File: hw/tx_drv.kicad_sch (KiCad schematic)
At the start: 7 parts, among them U35 SN75176AD

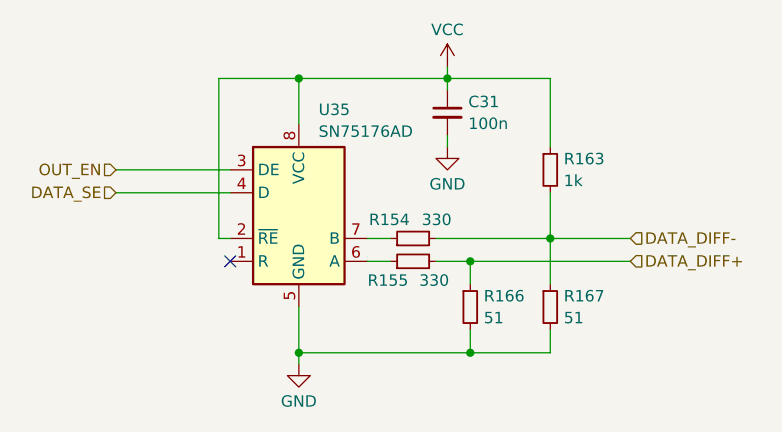
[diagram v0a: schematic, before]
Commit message: BUS*B* Parity bit driver direction pin was accidentally connected to BUS*A* direction net
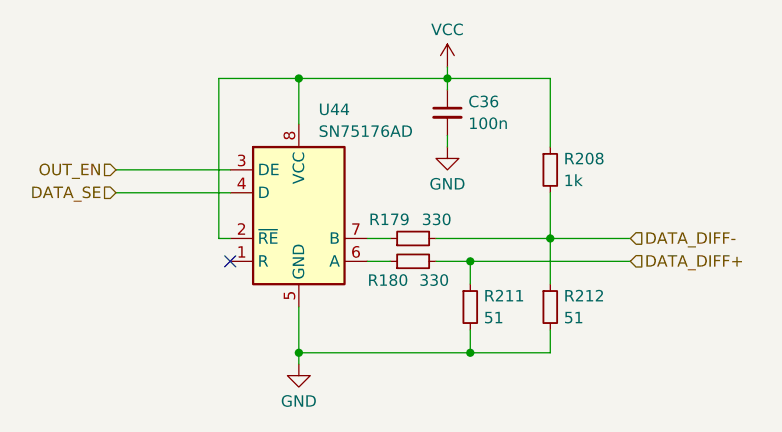
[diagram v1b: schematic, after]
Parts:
- renumbered C31 to C36, R154 to R179, R155 to R180, R163 to R208, R166 to R211, R167 to R212, U35 to U44
